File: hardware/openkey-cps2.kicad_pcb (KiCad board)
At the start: 2 copper layers, 23.3 x 23 mm, 14 parts, among them CN9 Conn_01x06, J1 Solder Pad, U1 ATtinyxx4

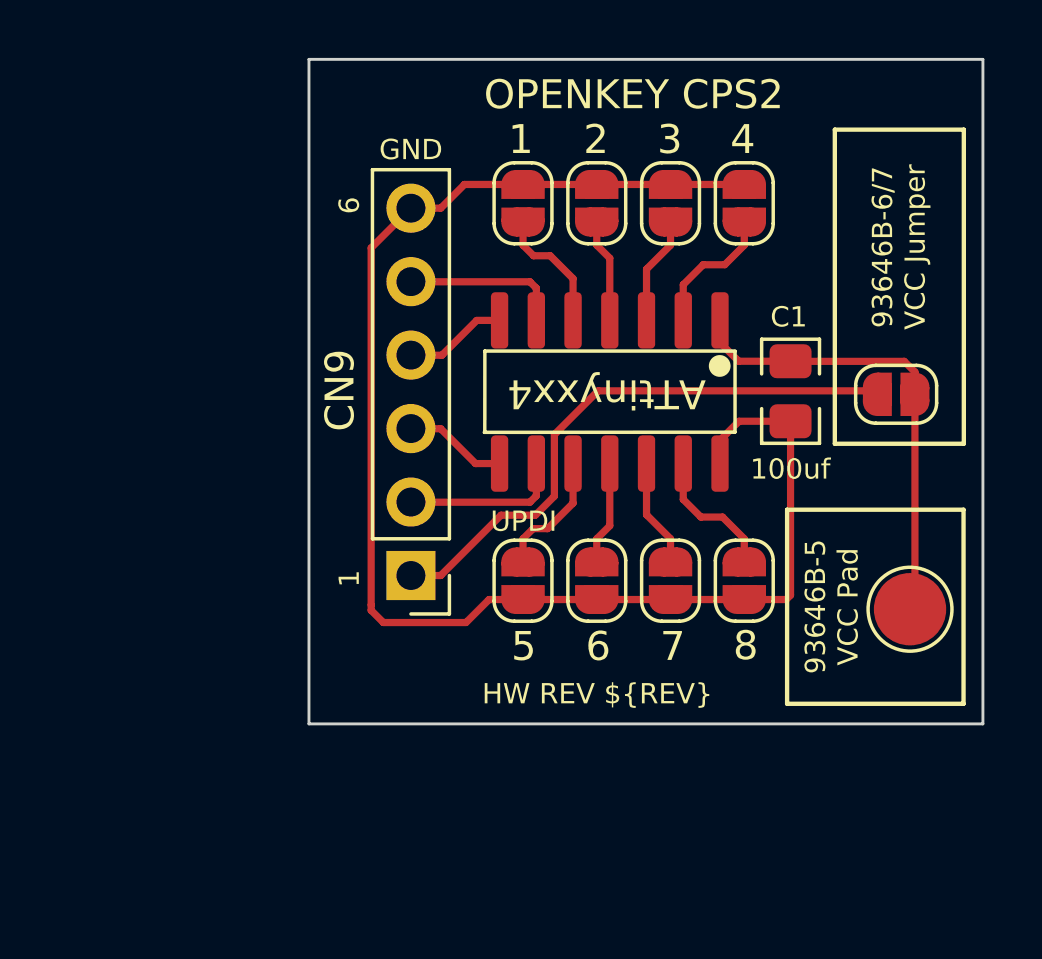
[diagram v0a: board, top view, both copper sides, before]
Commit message: Initial support for 93646B-3/4 revision boards
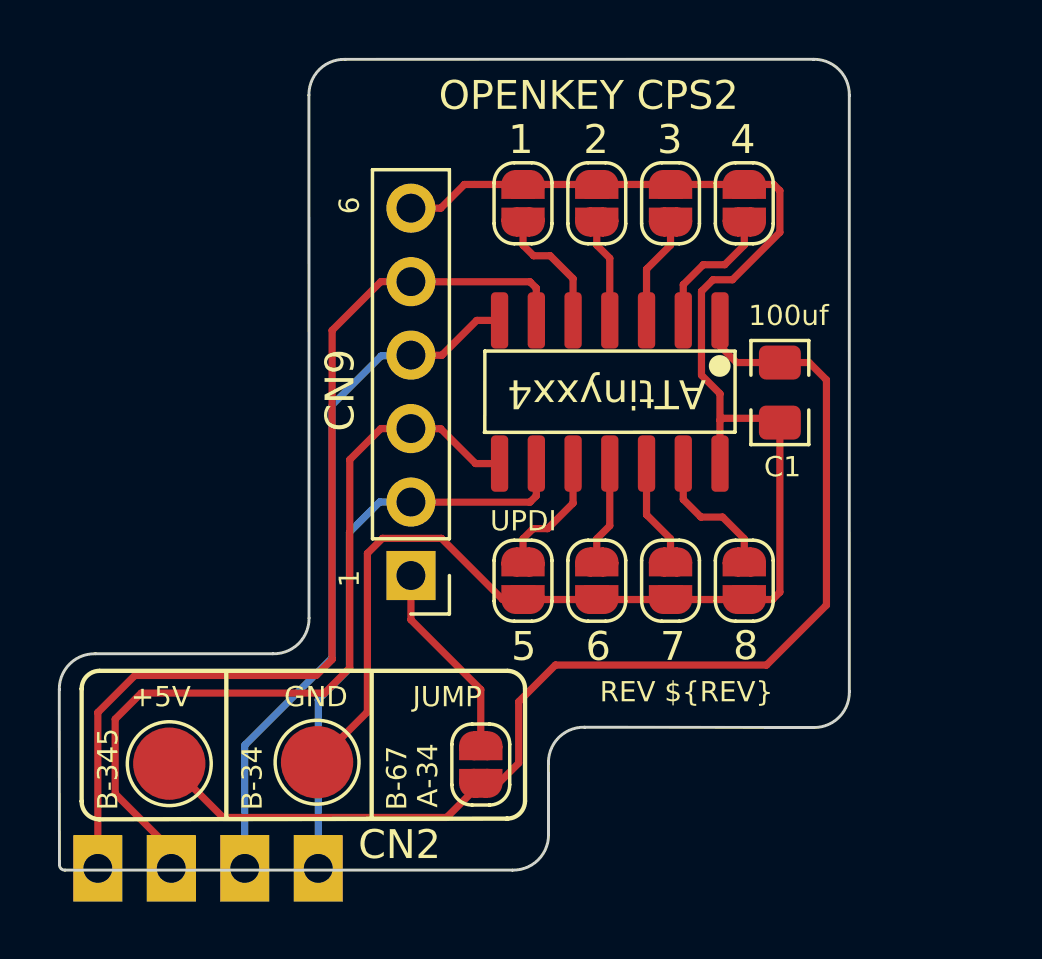
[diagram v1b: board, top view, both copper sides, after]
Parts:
- added J2: CN2, Connector_PinHeader_2.54mm:PinHeader_1x04_P2.54mm_Vertical, F.Cu at (116.7, 113.8)
- added J3: GND Pad, TestPoint:TestPoint_Pad_D2.5mm, F.Cu at (116.7, 110.1)
- J1: value Solder Pad -> VCC Pad
- moved J1 26.2 mm to (111.6, 110.2), turned to 90 degrees
- moved JP9 19.2 mm to (122.3, 110.2), turned to -90 degrees
- moved C1 0.37 mm to (132.7, 97.3)
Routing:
- net RESET: track 5.44 -> 34.4 mm
- net VCC: track 16.3 -> 40.6 mm
- net SETUP: track 3.56 -> 27.5 mm
- net CLOCK: track 3.56 -> 24.2 mm
- net DATA: track 5.44 -> 20.0 mm
- net /CN9 VCC: track 20.0 -> 6.89 mm
- net GND: track 50.9 -> 55.8 mm
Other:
- board size 23.3 x 23 mm -> 27.3 x 28 mm
- board text added: "+5V"
- board text added: "A-34"
- board text added: "B-34"
- board text added: "B-345"
- board text added: "B-67"
- board text added: "JUMP"
- board text added: "REV ${REV}"
- board text removed: "93646B-5 VCC Pad"
- board text removed: "93646B-6/7 VCC Jumper"

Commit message: HW: Add support for 93646B-3/4 and 97691A-3/4.  Add UPDI header.
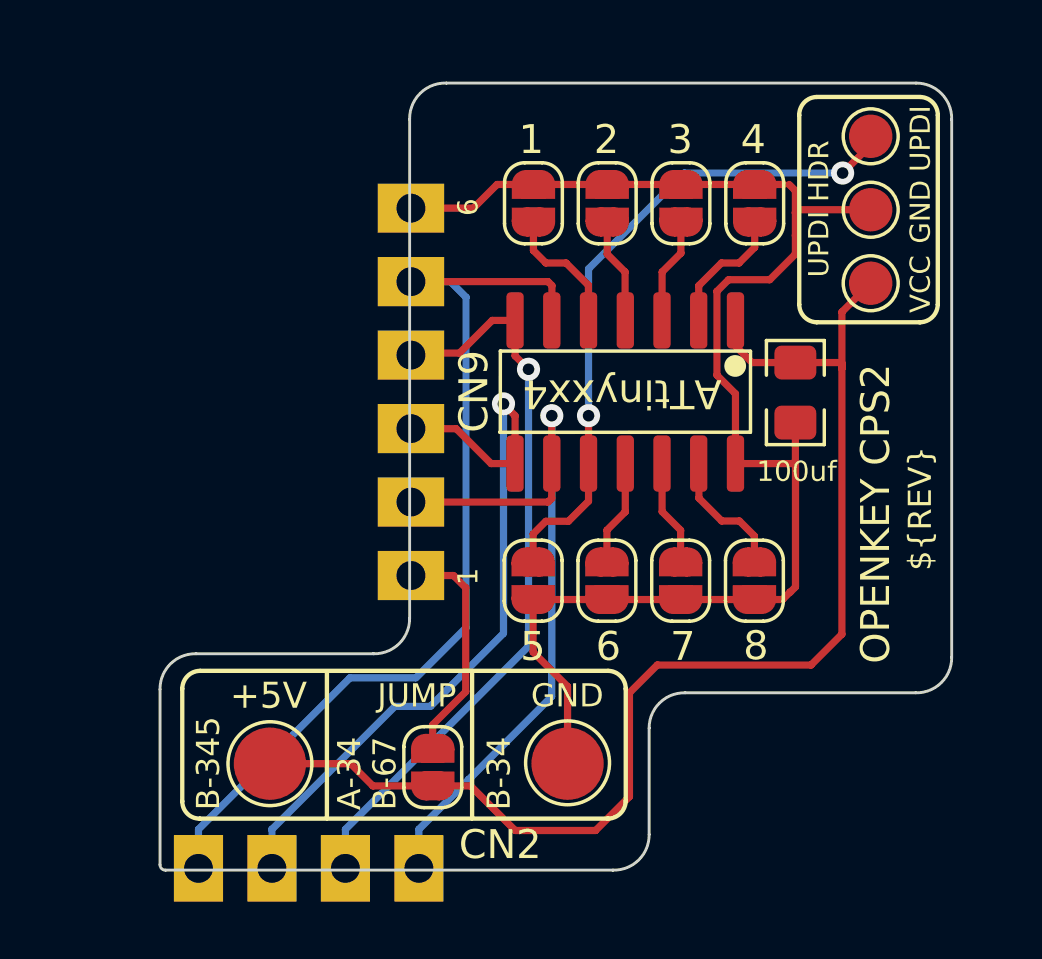
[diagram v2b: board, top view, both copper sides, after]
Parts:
- added J4: VCC, TestPoint:TestPoint_Pad_D1.5mm, F.Cu at (135.8, 93.5)
- added J5: GND, TestPoint:TestPoint_Pad_D1.5mm, F.Cu at (135.8, 91.0)
- added J6: J5 / UDPI, TestPoint:TestPoint_Pad_D1.5mm, F.Cu at (135.8, 88.5)
- moved J3 8.66 mm to (125.3, 110.1)
- moved J1 3.48 mm to (115.1, 110.2)
- moved J2 3.48 mm to (120.2, 113.8)
- moved REF** 2.34 mm to (129.9, 98.2)
- moved JP9 1.66 mm to (120.7, 110.3)
- moved C1 0.53 mm to (133.2, 97.3)
- moved U1 0.53 mm to (127.3, 97.3)
- moved JP5 0.36 mm to (131.8, 90.8)
- moved JP7 0.36 mm to (126.7, 90.8)
- moved JP8 0.36 mm to (124.2, 90.8)
- moved JP6 0.36 mm to (129.3, 90.8)
- moved JP4 0.35 mm to (131.8, 103.8)
- moved JP1 0.35 mm to (124.2, 103.8)
- moved JP2 0.35 mm to (126.7, 103.8)
- moved JP3 0.35 mm to (129.2, 103.8)
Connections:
- net /J5 renamed /J5 / UPDI
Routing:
- net /J5 / UPDI: track 4.41 -> 23.2 mm, vias 0 -> 2
- net GND: track 55.8 -> 50.0 mm
- net DATA: track 20.0 -> 25.2 mm, vias 0 -> 1
- net VCC: track 40.6 -> 43.2 mm
- net RESET: track 34.4 -> 32.0 mm
- net CLOCK: track 24.2 -> 25.7 mm, vias 0 -> 1
- net SETUP: track 27.5 -> 26.3 mm, vias 0 -> 1
- net /CN9 VCC: track 6.89 -> 8.01 mm
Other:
- board size 27.3 x 28 mm -> 27.4 x 27.2 mm
- board text added: "${REV}"
- board text added: "UPDI HDR"
- board text added: "VCC"
- board text removed: "REV ${REV}"
